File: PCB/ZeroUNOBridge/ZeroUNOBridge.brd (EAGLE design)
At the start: 33 x 64.4 mm, 19 parts, among them J1 RASPBERRYPI-40-PIN-GPIO, U1 ATMEGA328P_PDIP_EZ

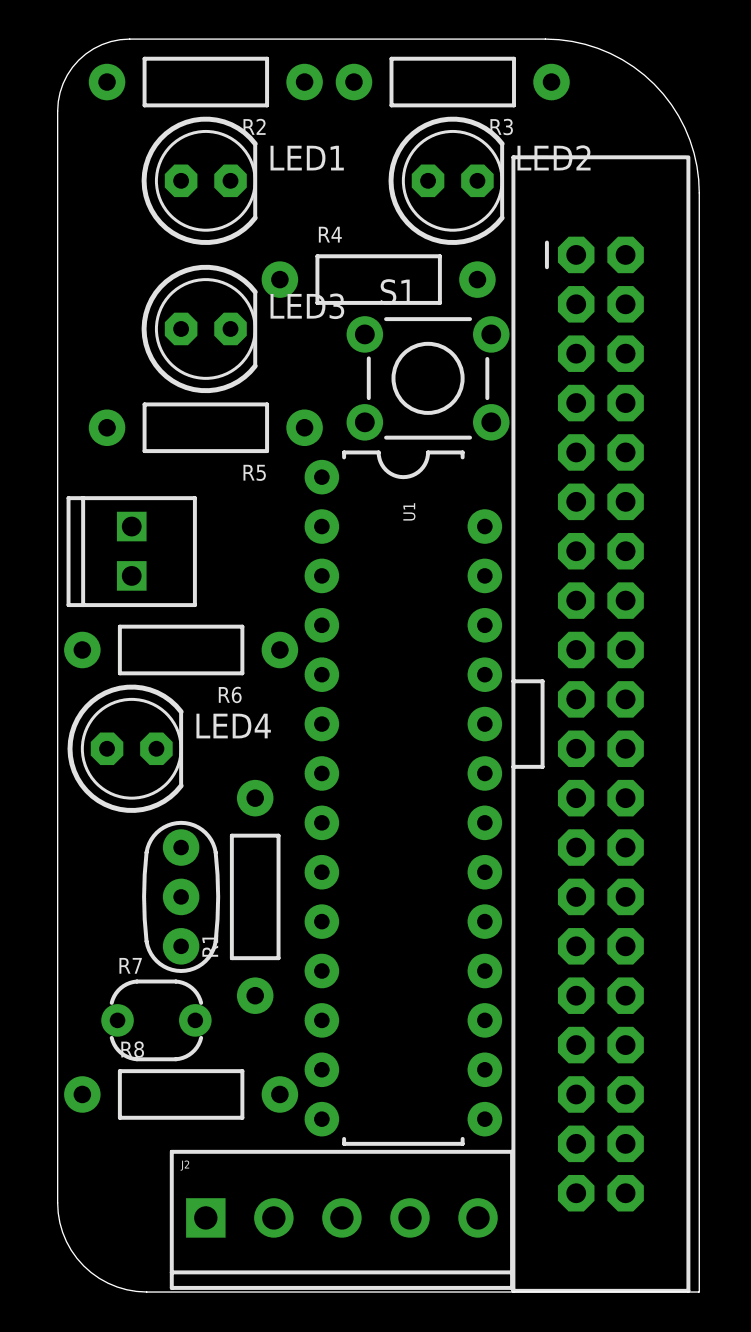
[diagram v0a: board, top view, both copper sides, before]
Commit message: Routing Traces
-Initial routing of traces
-Correcting component labels
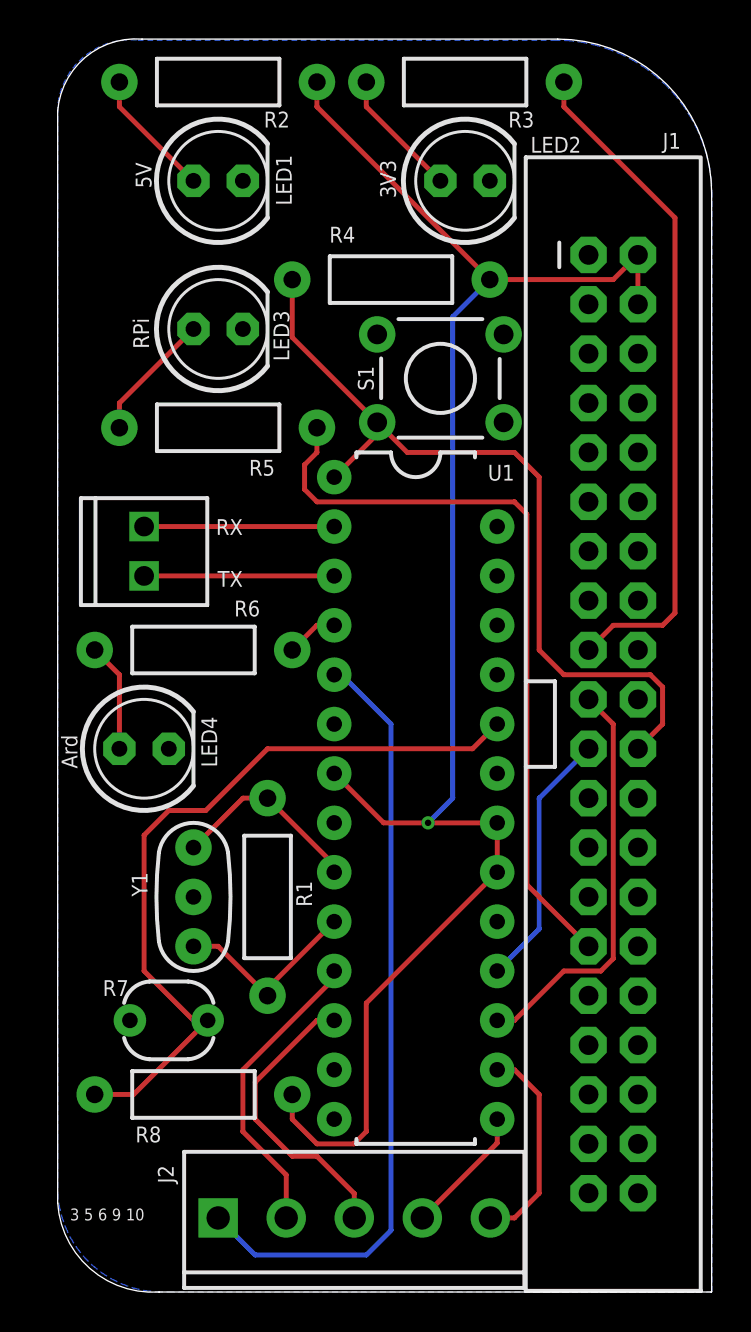
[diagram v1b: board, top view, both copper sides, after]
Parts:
- moved J2 0.64 mm to (8.26, 3.81)
- moved LED1 0.64 mm to (8.26, 57.1)
- moved LED3 0.64 mm to (8.26, 49.5)
- moved R2 0.64 mm to (8.26, 62.2)
- moved R5 0.64 mm to (8.26, 44.5)
- moved R6 0.64 mm to (6.99, 33.0)
- moved R8 0.64 mm to (6.99, 10.2)
- moved Y1 0.64 mm to (6.99, 20.3)
- moved J3 0.64 mm to (4.45, 36.8)
- moved LED4 0.64 mm to (4.45, 27.9)
- moved R1 0.63 mm to (10.8, 20.3)
- moved R7 0.63 mm to (5.71, 14.0)
- moved J1 0.63 mm to (28.6, 29.2)
- moved LED2 0.63 mm to (21.0, 57.1)
- moved R3 0.63 mm to (21.0, 62.2)
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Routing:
- net 5V: track 0.00 -> 87.7 mm, vias 0 -> 1
- net RESET: track 0.00 -> 42.1 mm
- net PIN3~: track 0.00 -> 40.2 mm
- net N$9: track 0.00 -> 39.2 mm
- net N$2: track 0.00 -> 38.9 mm
- net N$1: track 0.00 -> 34.9 mm
- net MOSI: track 0.00 -> 21.1 mm
- net PIN5~: track 0.00 -> 15.6 mm
- net PIN6~: track 0.00 -> 15.2 mm
- net MISO: track 0.00 -> 13.4 mm
- net PIN10~: track 0.00 -> 10.8 mm
- net XTAL2: track 0.00 -> 10.1 mm
- net XTAL1: track 0.00 -> 10.1 mm
- net TX: track 0.00 -> 9.78 mm
- net RX: track 0.00 -> 9.78 mm
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- added copper zone on layer 16, net GND
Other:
- board size 33 x 64.4 mm -> 33.6 x 64.5 mm
- board text added: "3 5 6 9 10"
- board text added: "3V3"
- board text added: "5V"
- board text added: "Ard"
- board text added: "RPi"
- board text added: "RX"
- board text added: "TX"
- board text added: "Y1"

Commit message: Added Power Jack
-Changed RPi port to compensate
-Adjusted labels
-Added tag
-Added initials
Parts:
- added J4: (no value), SparkFun-Connectors:1X02_2.54_SCREWTERM
- moved J1 3.45 mm to (27.6, 25.9)
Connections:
- removed net N$8: LED4.K
- net 5V: now also J4.P1
- net GND: now also J4.P2, LED4.K
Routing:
- net 5V: track 87.7 -> 83.3 mm
- net MISO: track 13.4 -> 9.65 mm
- net N$2: track 38.9 -> 41.8 mm
- net RESET: track 42.1 -> 44.8 mm
- net N$1: track 34.9 -> 37.4 mm
- net MOSI: track 21.1 -> 19.3 mm
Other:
- board size 33.6 x 64.5 mm -> 31.1 x 64.5 mm
- board text added: "+"
- board text added: "5V in"
- board text added: "KJW & BGR 7/2016"

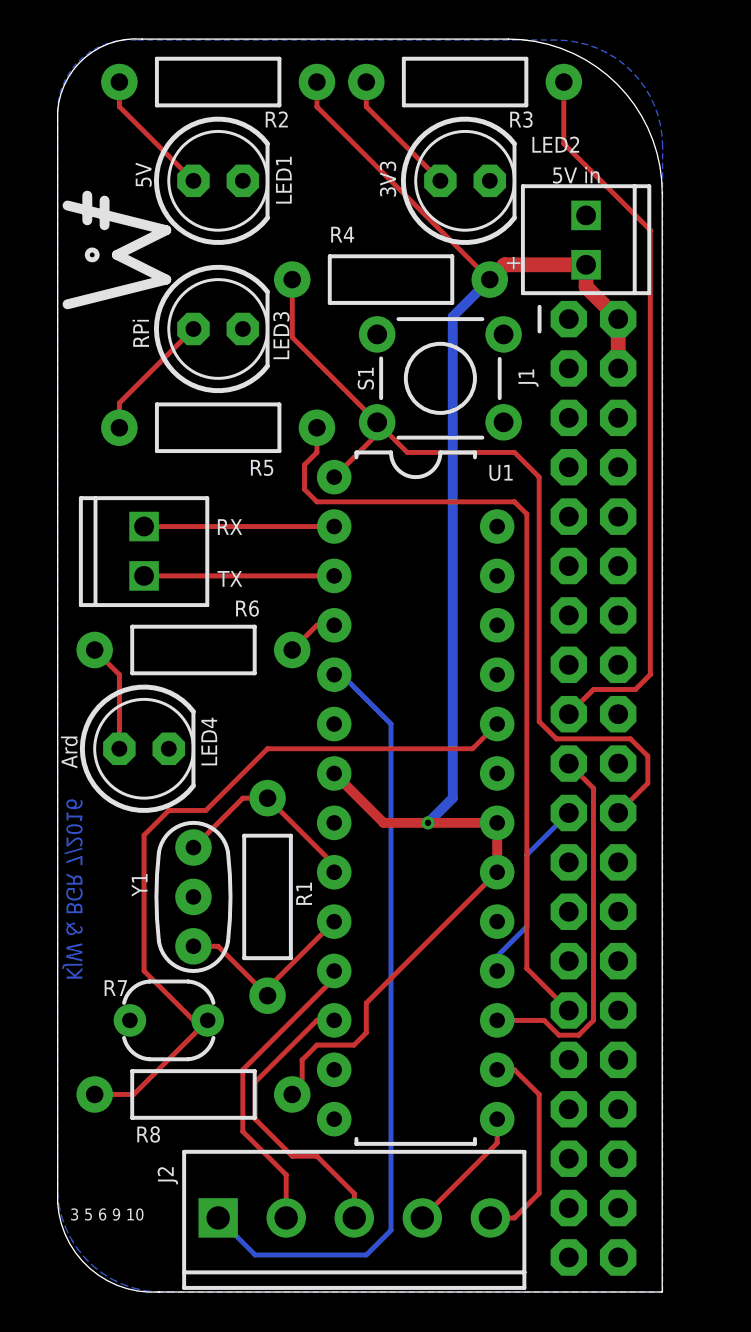
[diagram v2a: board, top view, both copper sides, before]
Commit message: Final Labeling Corrections
-Labeling jacks
-Added tag
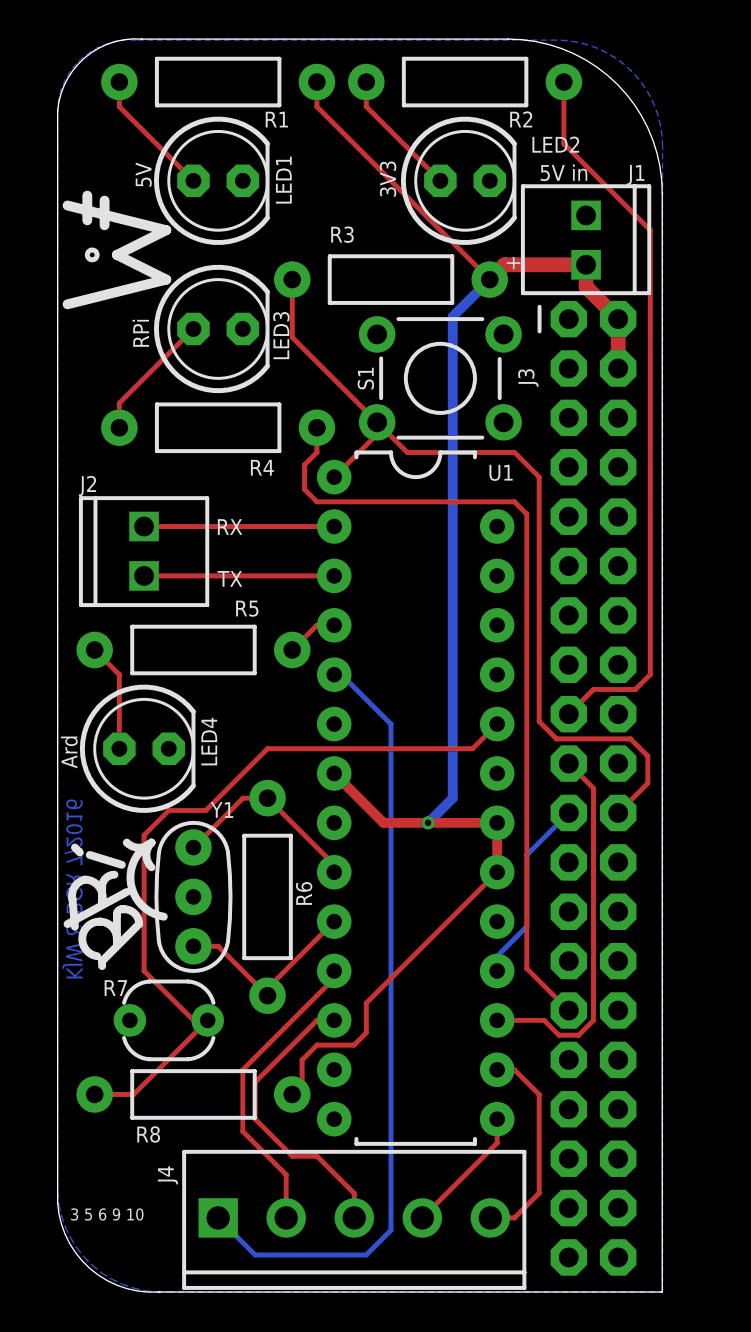
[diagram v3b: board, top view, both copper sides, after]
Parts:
- removed FRAME1: FRAME-LEDGER, SparkFun-Aesthetics:CREATIVE_COMMONS
- J1: value RASPBERRYPI-40-PIN-GPIO -> (none); device SparkFun-Boards:2X20-SHROUDED -> SparkFun-Connectors:1X02_2.54_SCREWTERM
- J2: device SparkFun-Connectors:SCREWTERMINAL-3.5MM-5 -> SparkFun-Connectors:1X02_2.54_SCREWTERM
- J3: value (none) -> RASPBERRYPI-40-PIN-GPIO; device SparkFun-Connectors:1X02_2.54_SCREWTERM -> SparkFun-Boards:2X20-SHROUDED
- J4: device SparkFun-Connectors:1X02_2.54_SCREWTERM -> SparkFun-Connectors:SCREWTERMINAL-3.5MM-5
- moved J4 54.9 mm to (8.26, 3.81), turned to 0 degrees
- moved R1 42.0 mm to (8.26, 62.2), turned to 180 degrees
- moved J2 33.2 mm to (4.45, 36.8), turned to 90 degrees
- moved J1 29.5 mm to (27.2, 55.4), turned to 270 degrees
- moved J3 25.6 mm to (27.6, 25.9), turned to 0 degrees
- moved R6 13.3 mm to (10.8, 20.3), turned to 90 degrees
- moved R2 12.7 mm to (21.0, 62.2)
- moved R4 11.7 mm to (8.26, 44.5), turned to 180 degrees
- moved R5 11.5 mm to (6.99, 33.0)
- moved R3 10.9 mm to (17.1, 52.1), turned to 0 degrees
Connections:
- net 3.3V: now also J3.1; no longer J1.1
- net 5V: now also J1.P1, J3.2, J3.4, R1.P$1, R3.P$2; no longer J1.2, J1.4, J4.P1, R2.P$1, R4.P$2
- net GND: now also J1.P2, J3.14, J3.20, J3.25, J3.30, J3.34, J3.39, J3.6, J3.9; no longer J1.14, J1.20, J1.25, J1.30, J1.34, J1.39, J1.6, J1.9, J4.P2
- net MISO: now also J3.21; no longer J1.21
- net MOSI: now also J3.19; no longer J1.19
- net N$1: now also J3.17, R2.P$1; no longer J1.17, R3.P$1
- net N$2: now also J3.29, R4.P$1; no longer J1.29, R5.P$1
- net N$3: now also R1.P$2; no longer R2.P$2
- net N$4: now also R2.P$2; no longer R3.P$2
- net N$5: now also R4.P$2; no longer R5.P$2
- net N$6: now also R5.P$1; no longer R6.P$1
- net N$7: now also R5.P$2; no longer R6.P$2
- net PIN10~: now also J4.5; no longer J2.5
- net PIN3~: now also J4.1; no longer J2.1
- net PIN5~: now also J4.2; no longer J2.2
- net PIN6~: now also J4.3; no longer J2.3
- net PIN9~: now also J4.4; no longer J2.4
- net RESET: now also J3.22, R3.P$1; no longer J1.22, R4.P$1
- net RX: now also J2.P1; no longer J3.P1
- net SCLK: now also J3.23; no longer J1.23
- net TX: now also J2.P2; no longer J3.P2
- net XTAL1: now also R6.P$2; no longer R1.P$2
- net XTAL2: now also R6.P$1; no longer R1.P$1
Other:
- board text added: "J1"
- board text added: "J2"

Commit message: Moved board width inwards
Should move left side in a bit as well
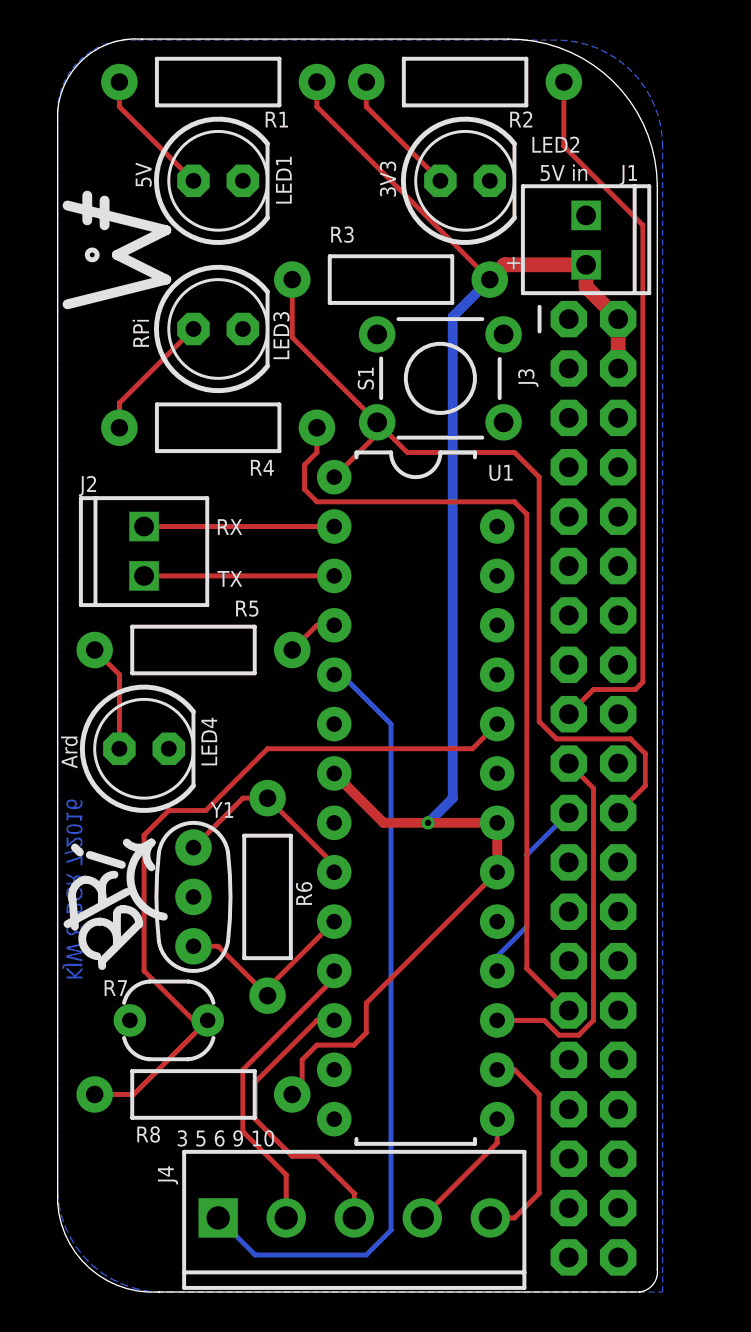
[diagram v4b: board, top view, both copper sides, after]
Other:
- board size 31.1 x 64.5 mm -> 30.8 x 64.5 mm
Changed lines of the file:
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@@
 <wire x1="0" y1="60.735503125" x2="0" y2="4.57905" width="0" layer="20"/>
 <wire x1="0" y1="4.57905" x2="5.21405" y2="0" width="0" layer="20" curve="90"/>
-<wire x1="5.21405" y1="0" x2="31.075" y2="0" width="0" layer="20"/>
-<wire x1="31.075" y1="0" x2="31.095" y2="0.02" width="0" layer="20" curve="90"/>
-<wire x1="31.095" y1="0.02" x2="31.095" y2="56.526" width="0" layer="20"/>
-<wire x1="31.095" y1="56.526" x2="23.181" y2="64.44" width="0" layer="20" curve="90"/>
+<wire x1="5.21405" y1="0" x2="29.932" y2="0" width="0" layer="20"/>
+<wire x1="29.932" y1="0" x2="30.841" y2="1.163" width="0" layer="20" curve="90"/>
+<wire x1="30.841" y1="1.163" x2="30.841" y2="56.907" width="0" layer="20"/>
+<wire x1="30.841" y1="56.907" x2="23.181" y2="64.44" width="0" layer="20" curve="90"/>
 <wire x1="23.181" y1="64.44" x2="4.339496875" y2="64.44" width="0" layer="20"/>
 <wire x1="4.339496875" y1="64.44" x2="0" y2="60.735503125" width="0" layer="20" curve="90"/>
@@
 <text x="4.826" y="56.769" size="0.8128" layer="25" font="vector" ratio="12" rot="R90">5V</text>
 <text x="4.699" y="48.514" size="0.8128" layer="25" font="vector" ratio="12" rot="R90">RPi</text>
-<text x="0.635" y="3.683" size="0.6096" layer="25" font="vector" ratio="12">3 5 6 9 10</text>
+<text x="6.096" y="7.493" size="0.8128" layer="25" font="vector" ratio="12">3 5 6 9 10</text>
 <text x="9.525" y="39.751" size="0.8128" layer="25" font="vector" ratio="12" rot="R180">RX</text>
 <text x="9.525" y="37.084" size="0.8128" layer="25" font="vector" ratio="12" rot="R180">TX</text>
@@
 <wire x1="0.889" y1="18.796" x2="0.762" y2="20.193" width="0.4064" layer="25"/>
 <text x="1.143" y="41.148" size="0.8128" layer="25" font="vector" ratio="12">J2</text>
-<text x="29.337" y="57.15" size="0.8128" layer="25" font="vector" ratio="12">J1</text>
+<text x="28.956" y="57.15" size="0.8128" layer="25" font="vector" ratio="12">J1</text>
 </plain>
 <attributes>
@@
 <wire x1="24.765" y1="29.337" x2="25.654" y2="28.448" width="0.254" layer="1"/>
 <wire x1="25.654" y1="28.448" x2="29.464" y2="28.448" width="0.254" layer="1"/>
-<wire x1="29.464" y1="28.448" x2="30.353" y2="27.559" width="0.254" layer="1"/>
-<wire x1="30.353" y1="27.559" x2="30.353" y2="26.162" width="0.254" layer="1"/>
-<wire x1="30.353" y1="26.162" x2="28.829" y2="24.638" width="0.254" layer="1"/>
+<wire x1="29.464" y1="28.448" x2="30.226" y2="27.686" width="0.254" layer="1"/>
+<wire x1="30.226" y1="27.686" x2="30.226" y2="26.035" width="0.254" layer="1"/>
+<wire x1="30.226" y1="26.035" x2="28.829" y2="24.638" width="0.254" layer="1"/>
 </signal>
 <signal name="SCLK">
@@
 <contactref element="J3" pad="17"/>
 <contactref element="R2" pad="P$1"/>
-<wire x1="26.035" y1="62.23" x2="26.035" y2="59.055" width="0.254" layer="1"/>
-<wire x1="26.035" y1="59.055" x2="30.48" y2="54.61" width="0.254" layer="1"/>
-<wire x1="30.48" y1="54.61" x2="30.48" y2="31.75" width="0.254" layer="1"/>
-<wire x1="30.48" y1="31.75" x2="29.718" y2="30.988" width="0.254" layer="1"/>
+<wire x1="26.035" y1="62.23" x2="26.035" y2="58.928" width="0.254" layer="1"/>
 <wire x1="29.718" y1="30.988" x2="27.559" y2="30.988" width="0.254" layer="1"/>
 <wire x1="27.559" y1="30.988" x2="26.289" y2="29.718" width="0.254" layer="1"/>
+<wire x1="26.035" y1="58.928" x2="30.099" y2="54.864" width="0.254" layer="1"/>
+<wire x1="30.099" y1="54.864" x2="30.099" y2="31.369" width="0.254" layer="1"/>
+<wire x1="30.099" y1="31.369" x2="29.718" y2="30.988" width="0.254" layer="1"/>
 </signal>
 <signal name="N$2">

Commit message: Misc Fixes
-Made board dimensions smaller
-Moved Bri's tag
-Actually connected up the SPI clock
-Moved 3.3V LED to other 3.3V port on RPi header
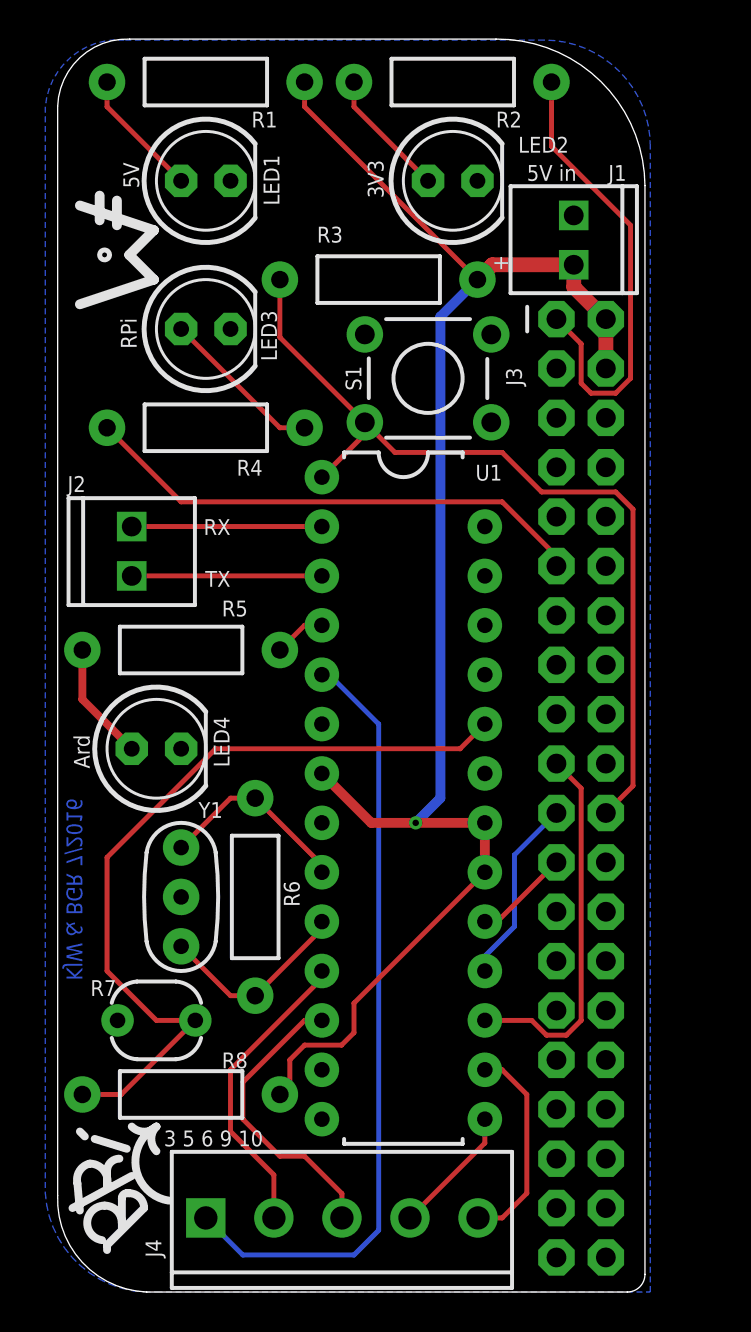
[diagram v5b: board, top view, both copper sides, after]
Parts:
- moved J1 0.64 mm to (26.5, 55.4)
- moved J3 0.64 mm to (26.9, 25.9)
- moved J4 0.64 mm to (7.62, 3.81)
- moved LED1 0.64 mm to (7.62, 57.1)
- moved LED3 0.64 mm to (7.62, 49.5)
- moved R1 0.64 mm to (7.62, 62.2)
- moved R4 0.64 mm to (7.62, 44.5)
- moved R5 0.64 mm to (6.35, 33.0)
- moved R8 0.64 mm to (6.35, 10.2)
- moved Y1 0.64 mm to (6.35, 20.3)
- moved J2 0.64 mm to (3.81, 36.8)
- moved LED4 0.63 mm to (5.08, 27.9)
- moved R6 0.63 mm to (10.2, 20.3)
- moved R7 0.63 mm to (5.08, 14.0)
- moved LED2 0.63 mm to (20.3, 57.1)
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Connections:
- removed net SCK: U1.19
- net 3.3V: now also J3.17; no longer J3.1
- net N$1: now also J3.1; no longer J3.17
- net N$2: now also J3.11, R4.P$2; no longer J3.29, R4.P$1
- net N$5: now also R4.P$1; no longer R4.P$2
- net SCLK: now also U1.19
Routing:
- net N$2: track 41.8 -> 26.4 mm
- net N$1: track 37.0 -> 23.8 mm
- net SCLK: track 0.00 -> 4.95 mm
- net N$9: track 39.2 -> 41.1 mm
- net N$5: track 6.66 -> 8.45 mm
- net N$7: track 5.61 -> 6.13 mm
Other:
- board size 30.8 x 64.5 mm -> 30.2 x 64.4 mm
